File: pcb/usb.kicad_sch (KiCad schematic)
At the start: 31 parts, among them J17 USB_B_Mini, Q22 PMOS, Q23 PMOS, Q25 NMOS, Q27 PMOS, U15 FT230XQ, U19 Conn_02x03_Counter_Clockwise

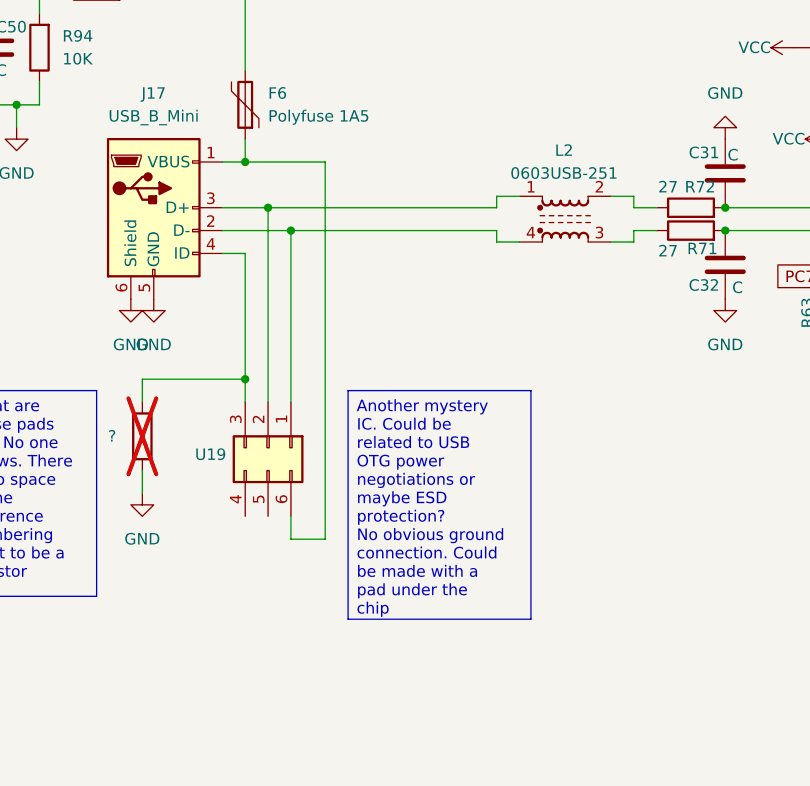
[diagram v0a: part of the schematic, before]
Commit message: Add the last few mystery components to the schematic, update the licence and start on RHSP
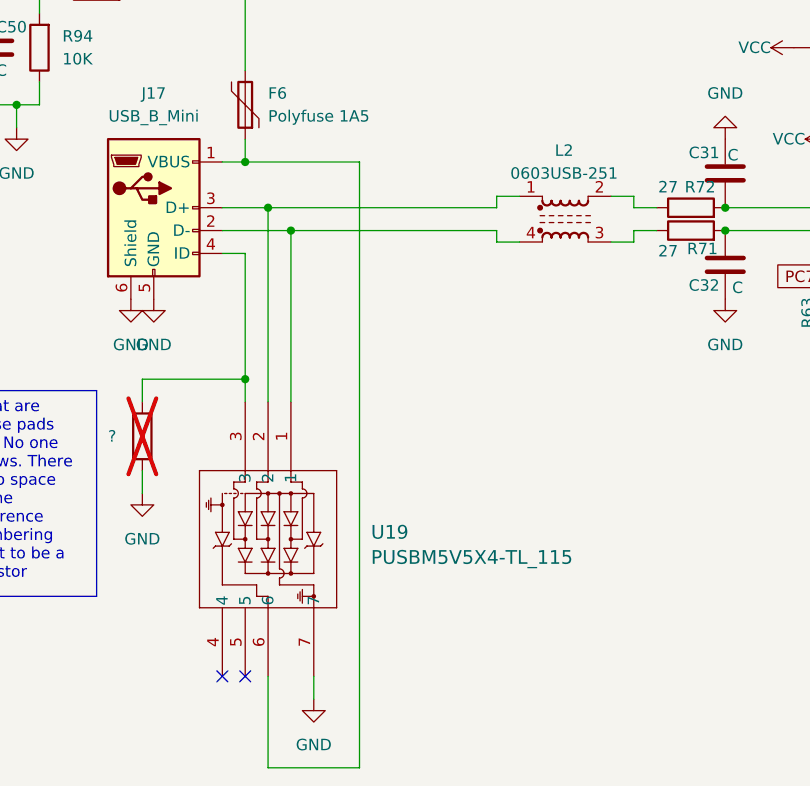
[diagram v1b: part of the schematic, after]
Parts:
- removed U19: Conn_02x03_Counter_Clockwise, symbol Connector_Generic:Conn_02x03_Counter_Clockwise
- added U19: PUSBM5V5X4-TL_115, DFN1616-6_SOT1189-1_NEX, symbol PUSBM5V5X4_TL_115:PUSBM5V5X4-TL_115
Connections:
- net GND: now also U19.7
- net at J17.3 (D+), L2.1: now also U19.2
- net at J17.2 (D-), L2.4: now also U19.1
- net at J17.4 (ID), R?.1: now also U19.3
- net at F6.1, J17.1 (VBUS): now also U19.6
- no-connect marks 0 -> 2
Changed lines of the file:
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@@
 		)
 	)
-	(text_box "Another mystery IC. Could be related to USB OTG power negotiations or maybe ESD protection?\nNo obvious ground connection. Could be made with a pad under the chip"
-		(exclude_from_sim no)
-		(at 139.7 137.16 0)
-		(size 20.32 25.4)
-		(margins 0.9525 0.9525 0.9525 0.9525)
-		(stroke
-			(width 0)
-			(type solid)
-		)
-		(fill
-			(type none)
-		)
-		(effects
-			(font
-				(size 1.27 1.27)
-			)
-			(justify left top)
-		)
-	)
 	(text_box "What are these pads for? No one knows. There is no space in the reference numbering for it to be a resistor"
 		(exclude_from_sim no)
@@
 		(color 0 0 0 0)
 	)
-	(wire
-		(pts
-			(xy 133.35 153.67) (xy 133.35 151.13)
-		)
-		(stroke
-			(width 0)
-			(type default)
-		)
+	(no_connect
+		(at 128.27 168.91)
+	)
+	(no_connect
+		(at 125.73 168.91)
 	)
 	(wire
@@
 	(wire
 		(pts
+			(xy 130.81 179.07) (xy 140.97 179.07)
+		)
+		(stroke
+			(width 0)
+			(type default)
+		)
+	)
+	(wire
+		(pts
 			(xy 125.73 116.84) (xy 130.81 116.84)
 		)
@@
 	(wire
 		(pts
-			(xy 128.27 111.76) (xy 137.16 111.76)
+			(xy 128.27 111.76) (xy 140.97 111.76)
 		)
 		(stroke
@@
 	(wire
 		(pts
+			(xy 130.81 168.91) (xy 130.81 179.07)
+		)
+		(stroke
+			(width 0)
+			(type default)
+		)
+	)
+	(wire
+		(pts
 			(xy 171.45 119.38) (xy 173.99 119.38)
 		)
@@
 	(wire
 		(pts
+			(xy 135.89 168.91) (xy 135.89 171.45)
+		)
+		(stroke
+			(width 0)
+			(type default)
+		)
+	)
+	(wire
+		(pts
 			(xy 125.73 67.31) (xy 128.27 67.31)
 		)
@@
 	(wire
 		(pts
-			(xy 137.16 111.76) (xy 137.16 153.67)
+			(xy 140.97 111.76) (xy 140.97 179.07)
 		)
 		(stroke
@@
 	(wire
 		(pts
-			(xy 137.16 153.67) (xy 133.35 153.67)
-		)
-		(stroke
-			(width 0)
-			(type default)
-		)
-	)
-	(wire
-		(pts
 			(xy 105.41 92.71) (xy 105.41 95.25)
 		)
@@
 	)
 	(symbol
+		(lib_id "PUSBM5V5X4_TL_115:PUSBM5V5X4-TL_115")
+		(at 133.35 138.43 270)
+		(unit 1)
+		(exclude_from_sim no)
+		(in_bom yes)
+		(on_board yes)
+		(dnp no)
+		(property "Reference" "U19"
+			(at 142.24 152.908 90)
+			(effects
+				(font
+					(size 1.524 1.524)
+				)
+				(justify left)
+			)
+		)
+		(property "Value" "PUSBM5V5X4-TL_115"
+			(at 142.24 155.702 90)
+			(effects
+				(font
+					(size 1.524 1.524)
+				)
+				(justify left)
+			)
+		)
+		(property "Footprint" "DFN1616-6_SOT1189-1_NEX"
+			(at 133.35 138.43 0)
+			(effects
+				(font
+					(size 1.27 1.27)
+					(italic yes)
+				)
+				(hide yes)
+			)
+		)
+		(property "Datasheet" "PUSBM5V5X4-TL_115"
+			(at 133.35 138.43 0)
+			(effects
+				(font
+					(size 1.27 1.27)
+					(italic yes)
+				)
+				(hide yes)
+			)
+		)
+		(property "Description" ""
+			(at 133.35 138.43 0)
+			(effects
+				(font
+					(size 1.27 1.27)
+				)
+				(hide yes)
+			)
+		)
+		(pin "4"
+		)
+		(pin "1"
+		)
+		(pin "2"
+		)
+		(pin "5"
+		)
+		(pin "3"
+		)
+		(pin "6"
+		)
+		(pin "7"
+		)
+		(instances
+			(project ""
+				(path "/a3d12dc7-033a-4c99-b909-7e1454b0334e/2852d2a3-22cd-4266-9d0c-f9eb62968661"
+					(reference "U19")
+					(unit 1)
+				)
+			)
+		)
+	)
+	(symbol
 		(lib_id "power:GND")
 		(at 196.85 99.06 90)
@@
 	)
 	(symbol
-		(lib_id "Connector_Generic:Conn_02x03_Counter_Clockwise")
-		(at 130.81 143.51 270)
-		(unit 1)
-		(exclude_from_sim no)
-		(in_bom yes)
-		(on_board yes)
-		(dnp no)
-		(property "Reference" "U19"
-			(at 122.682 144.272 90)
-			(effects
-				(font
-					(size 1.27 1.27)
-				)
-				(justify left)
-			)
-		)
-		(property "Value" "Conn_02x03_Counter_Clockwise"
-			(at 135.89 146.0499 90)
-			(effects
-				(font
-					(size 1.27 1.27)
-				)
-				(justify left)
-				(hide yes)
-			)
-		)
-		(property "Footprint" ""
-			(at 130.81 143.51 0)
-			(effects
-				(font
-					(size 1.27 1.27)
-				)
-				(hide yes)
-			)
-		)
-		(property "Datasheet" "~"
-			(at 130.81 143.51 0)
-			(effects
-				(font
-					(size 1.27 1.27)
-				)
-				(hide yes)
-			)
-		)
-		(property "Description" "Generic connector, double row, 02x03, counter clockwise pin numbering scheme (similar to DIP package numbering), script generated (kicad-library-utils/schlib/autogen/connector/)"
-			(at 130.81 143.51 0)
-			(effects
-				(font
-					(size 1.27 1.27)
-				)
-				(hide yes)
-			)
-		)
-		(pin "2"
-		)
-		(pin "5"
-		)
-		(pin "6"
-		)
-		(pin "3"
-		)
-		(pin "1"
-		)
-		(pin "4"
-		)
-		(instances
-			(project ""
-				(path "/a3d12dc7-033a-4c99-b909-7e1454b0334e/2852d2a3-22cd-4266-9d0c-f9eb62968661"
-					(reference "U19")
-					(unit 1)
-				)
-			)
-		)
-	)
-	(symbol
 		(lib_id "Device:R")
 		(at 231.14 105.41 0)
@@
 					(unit 1)
 				)
+			)
+		)
+	)
+	(symbol
+		(lib_id "power:GND")
+		(at 135.89 171.45 0)
+		(unit 1)
+		(exclude_from_sim no)
+		(in_bom yes)
+		(on_board yes)
+		(dnp no)
+		(fields_autoplaced yes)
+		(property "Reference" "#PWR023"
+			(at 135.89 177.8 0)
+			(effects
+				(font
+					(size 1.27 1.27)
+				)
+				(hide yes)
+			)
+		)
+		(property "Value" "GND"
+			(at 135.89 176.53 0)
+			(effects
+				(font
+					(size 1.27 1.27)
+				)
+			)
+		)
+		(property "Footprint" ""
+			(at 135.89 171.45 0)
+			(effects
+				(font
+					(size 1.27 1.27)
+				)
+				(hide yes)
+			)
+		)
+		(property "Datasheet" ""
+			(at 135.89 171.45 0)
+			(effects
+				(font
+					(size 1.27 1.27)
+				)
+				(hide yes)
+			)
+		)
+		(property "Description" "Power symbol creates a global label with name \"GND\" , ground"
+			(at 135.89 171.45 0)
+			(effects
+				(font
+					(size 1.27 1.27)
+				)
+				(hide yes)
+			)
+		)
+		(pin "1"
+		)
+		(instances
+			(project ""
+				(path "/a3d12dc7-033a-4c99-b909-7e1454b0334e/2852d2a3-22cd-4266-9d0c-f9eb62968661"
+					(reference "#PWR023")
+					(unit 1)
+				)

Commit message: Before tear out
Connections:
- no-connect marks 2 -> 3
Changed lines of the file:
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@@
+	)
+	(no_connect
+		(at 228.6 129.54)
 	)
 	(no_connect
